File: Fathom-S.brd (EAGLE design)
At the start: 112.4 x 45.7 mm, 114 parts, among them IC1 LMH6643, IC2 LMH6643, IC3 ST490AB, IC4 ST490AB, IC5 FT230XS, Q1 BC817-40W, U1 MC7812, U2 MC7805, U4 INA139, U5 MC7805, X2 USBSMD

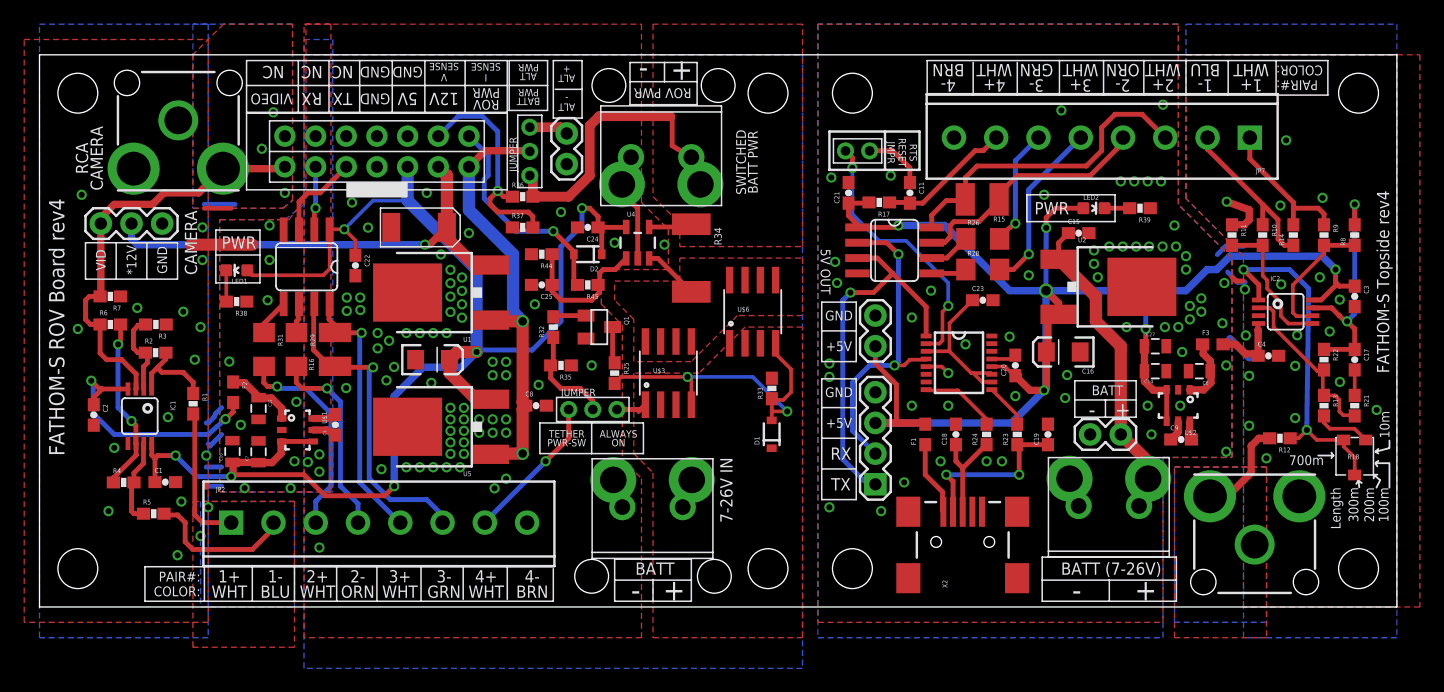
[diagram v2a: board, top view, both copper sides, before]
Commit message: Massive revision to simplify and make easier to use. Added DroneCode connectors, removed excessive stuff, and removed power switching.
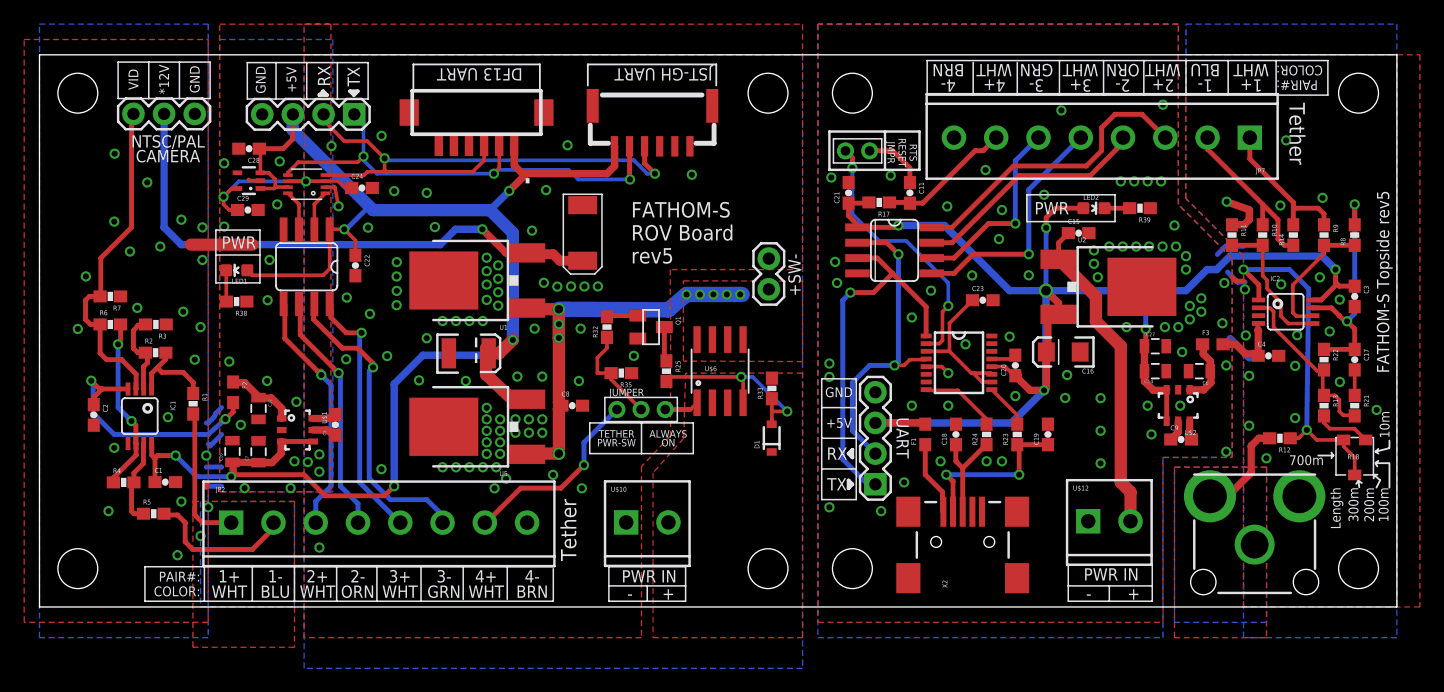
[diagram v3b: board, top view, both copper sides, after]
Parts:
- removed C25: 0.1uF, SparkFun-Passives:0603-CAP
- removed D2: Schottky, SparkFun-DiscreteSemi:SOD-323
- removed JP10, JP4, JP9: 0.1" HEADER, SparkFun-Connectors:1X02
- removed R15, R16: NP, resistor:R1210
- removed R26, R28, R29, R31: 0, SparkFun:1206
- removed R34: 0.001 1% 3W, SparkFun-Resistors:R2512
- removed R36: 18K 1%, SparkFun-Resistors:0603-RES
- removed R37: 2.2K 1%, SparkFun-Resistors:0603-RES
- removed R44: 68K 1%, SparkFun-Resistors:0603-RES
- removed R45: 1K, SparkFun-Resistors:0603-RES
- removed U$14: HEADER-33MM, BlueRobotics-Main:HEADER-2MM-3POS
- removed U4: INA139, SparkFun-AnalogIC:SOT23-5
- added C28, C29: 1uF, SparkFun-Passives:0603-CAP
- added JP5: M02PTH, SparkFun-Connectors:1X02
- added U$15: VREG-MIC5365, BlueRobotics-Main:SC70-5L
- C10: value 10uF 16V -> 47uF 10V; device SparkFun-Passives:EIA3216 -> SparkFun-Passives:EIA3528
- C24: device SparkFun-Passives:0603-CAP -> SparkFun:0603-CAP
- JP1: value PJRAN1X1U04X -> (none); device BlueRobotics-Main:RCA -> SparkFun-Connectors:1X04
- U$10, U$12: value HEADER-2 -> M023.5MM; device BR-Eagle-Library:TETHER-POWER-TERMINALS -> SparkFun-Connectors:SCREWTERMINAL-3.5MM-2
- U$11: value HEADER-2 -> JST-GH-6TOP-ENTRY; device BR-Eagle-Library:TETHER-POWER-TERMINALS -> BlueRobotics-JST-GH:JST-GH-TOP-6
- U$3: value Si4459ADY -> DF13-6P-1.25V; device SparkFun-DiscreteSemi:SO08 -> con-hirose-df13:DF13C-6P-1.25V
- U$6: value Si4459ADY -> AO4407A
- U$8: value TETHER-HEADERSERIAL -> TXS0102DCUR; device BR-Eagle-Library:TETHER-HEADER-2X7 -> BlueRobotics-Main:VSSOP-8
- moved U$4 47.9 mm to (35.1, -0.79), turned to 0 degrees
- moved U$9 25.9 mm to (5.73, 32.3)
- moved U$3 25.4 mm to (36.2, 39.1), turned to 180 degrees
- moved C24 19.0 mm to (26.7, 34.7), turned to 0 degrees
- moved JP1 14.6 mm to (26.1, 40.8), turned to 180 degrees
- moved C13 13.5 mm to (45.0, 31.0), turned to 90 degrees
- moved JP3 9.47 mm to (12.9, 40.8)
- moved U$6 5.61 mm to (56.4, 19.5)
- moved R35 5.04 mm to (48.2, 19.4)
- moved R32 4.45 mm to (47.0, 23.2)
- moved R25 4.29 mm to (51.9, 19.5)
- moved Q1 4.29 mm to (50.6, 23.2)
- moved U$8 4.00 mm to (23.7, 34.3), turned to 90 degrees
- moved U$13 4.00 mm to (47.8, 16.4)
- moved U1 3.16 mm to (35.1, 27.0)
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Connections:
- removed net I_SENSE: D2.A, R45.2, U$8.I_SENSE
- removed net N$23: IC3.5, R28.1
- removed net N$24: IC4.5, R31.1
- removed net N$25: IC4.6, R29.1
- removed net N$26: IC3.6, R26.1
- removed net N$33: C25.1, R44.1, R45.1, U4.1
- removed net ROV-ALT-VIN: JP10.1, U$14.P$3
- removed net ROV-VIN-PRESENSE: R34.2, U$3.5, U$3.6, U$3.7, U$3.8, U$6.5, U$6.6, U$6.7, U$6.8, U4.3
- removed net ROV-VIN-SWITCHED: R34.1, R36.2, U$11.1A, U$11.1B, U$14.P$1, U4.4
- removed net V_SENSE: R36.1, R37.2, U$8.V_SENSE
- new net 3.3V-ISO: C24.1, C29.1, U$15.5, U$8.3, U$8.6
- new net RX-3.3V: JP1.2, U$11.3, U$3.P$3, U$8.4
- new net TX-3.3V: JP1.1, U$11.2, U$3.P$2, U$8.5
- net 12V-ISO: no longer U$8.12V
- net CAMERA: no longer JP1.PIN, U$8.VIDEO
- net GND: now also U$12.1; no longer JP4.2, JP9.2, U$12.1A, U$12.1B
- net GND-ISO: now also C28.2, C29.2, JP1.4, JP5.1, U$10.1, U$11.6, U$15.2, U$3.P$6, U$8.2; no longer C25.2, JP1.SHELL, JP10.2, R37.1, R44.2, U$10.1A, U$10.1B, U$11.2A, U$11.2B, U$8.GND0, U$8.GND1, U$8.GND2, U4.2
- net N$28: no longer U$3.4
- net ROV-BATT: now also U$10.2; no longer U$10.2A, U$10.2B, U$3.1, U$3.2, U$3.3
- net ROV-RX: now also U$8.1; no longer U$8.RX
- net ROV-TP2+: now also IC4.5; no longer R31.2
- net ROV-TP2-: now also IC4.6; no longer R29.2
- net ROV-TP3+: no longer R16.2
- net ROV-TP3-: no longer R16.1
- net ROV-TX: now also U$8.8; no longer U$8.TX
- net ROV-VIN: now also JP5.2, U$6.5, U$6.6, U$6.7, U$6.8; no longer U$14.P$2, U$8.VBAT
- net TOP-TP2+: no longer R15.2
- net TOP-TP2-: no longer R15.1
- net TOP-TP3+: now also IC3.5; no longer R28.2
- net TOP-TP3-: now also IC3.6; no longer R26.2
- net TOP-VIN: now also U$12.2; no longer JP9.1, U$12.2A, U$12.2B
- net VCC: no longer JP4.1
- net VCC-ISO: now also C28.1, JP1.3, U$11.1, U$15.1, U$15.3, U$3.P$1, U$8.7; no longer C24.1, D2.C, U$8.5V, U4.5
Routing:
- net RX-3.3V: track 0.00 -> 48.5 mm, vias 0 -> 2
- net TX-3.3V: track 0.00 -> 39.5 mm, vias 0 -> 3
- net ROV-VIN-SWITCHED: track 26.4 -> 0.00 mm
- net VCC-ISO: track 121.3 -> 140.6 mm
- net V_SENSE: track 18.7 -> 0.00 mm, vias 1 -> 0
- net I_SENSE: track 18.2 -> 0.00 mm, vias 1 -> 0
- net 3.3V-ISO: track 0.00 -> 16.3 mm, vias 0 -> 2
- net N$33: track 12.0 -> 0.00 mm
- net N$28: track 27.7 -> 16.9 mm
- net CAMERA: track 35.3 -> 27.9 mm
- net 12V-ISO: track 39.0 -> 46.2 mm
- net VCC: track 125.1 -> 117.9 mm
- net TOP-TP3-: track 9.83 -> 16.0 mm
- net GND-ISO: track 20.6 -> 14.6 mm, vias 94 -> 109
- net TOP-TP3+: track 14.4 -> 20.1 mm
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- added copper zone on layer 1, net ROV-VIN
- removed copper zone on layer 1, net ROV-VIN-PRESENSE
- removed copper zone on layer 1, net ROV-VIN-SWITCHED
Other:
- board text added: "+SW-"
- board text added: "4/16"
- board text added: "DF13 UART"
- board text added: "DroneCode Mini Compatible"
- board text added: "FATHOM-S ROV Board rev5"
- board text added: "FATHOM-S Topside rev5"
- board text added: "JST-GH UART"
- board text added: "NTSC/PAL CAMERA"
- board text added: "PWR IN"
- board text added: "Tether"
- board text added: "UART"
- board text removed: "12/15"
- board text removed: "12V"
- board text removed: "5V"
- board text removed: "5V OUT"
- board text removed: "7-26V IN"
- board text removed: "ALT +"
- board text removed: "ALT -"
- board text removed: "ALT PWR"
- board text removed: "BATT"
- board text removed: "BATT (7-26V)"
- board text removed: "BATT PWR"
- board text removed: "CAMERA"
- board text removed: "FATHOM-S ROV Board rev4"
- board text removed: "FATHOM-S Topside rev4"
- board text removed: "I SENSE"
- board text removed: "NC"
- board text removed: "RCA CAMERA"
- board text removed: "ROV PWR"
- board text removed: "SWITCHED BATT PWR"
- board text removed: "V SENSE"
- board text removed: "VIDEO"

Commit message: Change 12V output capacitor size.
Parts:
- C13: value 10uF 25V -> 33uF 20V
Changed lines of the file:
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@@
 <attribute name="VALUE" value="3.3V" x="60.6275" y="13.985" size="1.778" layer="27" rot="R90" display="off"/>
 </element>
-<element name="C13" library="SparkFun-Passives" package="EIA6032" value="10uF 25V" x="44.97375" y="30.9725" rot="R90"/>
+<element name="C13" library="SparkFun-Passives" package="EIA6032" value="33uF 20V" x="44.97375" y="30.9725" rot="R90"/>
 <element name="JP3" library="SparkFun-Connectors" package="1X03" value="0.1&quot; HEADER" x="12.85875" y="40.83" smashed="yes" rot="R180"/>
 <element name="U$6" library="SparkFun-DiscreteSemi" package="SO08" value=" AO4407A " x="56.35625" y="19.52625"/>

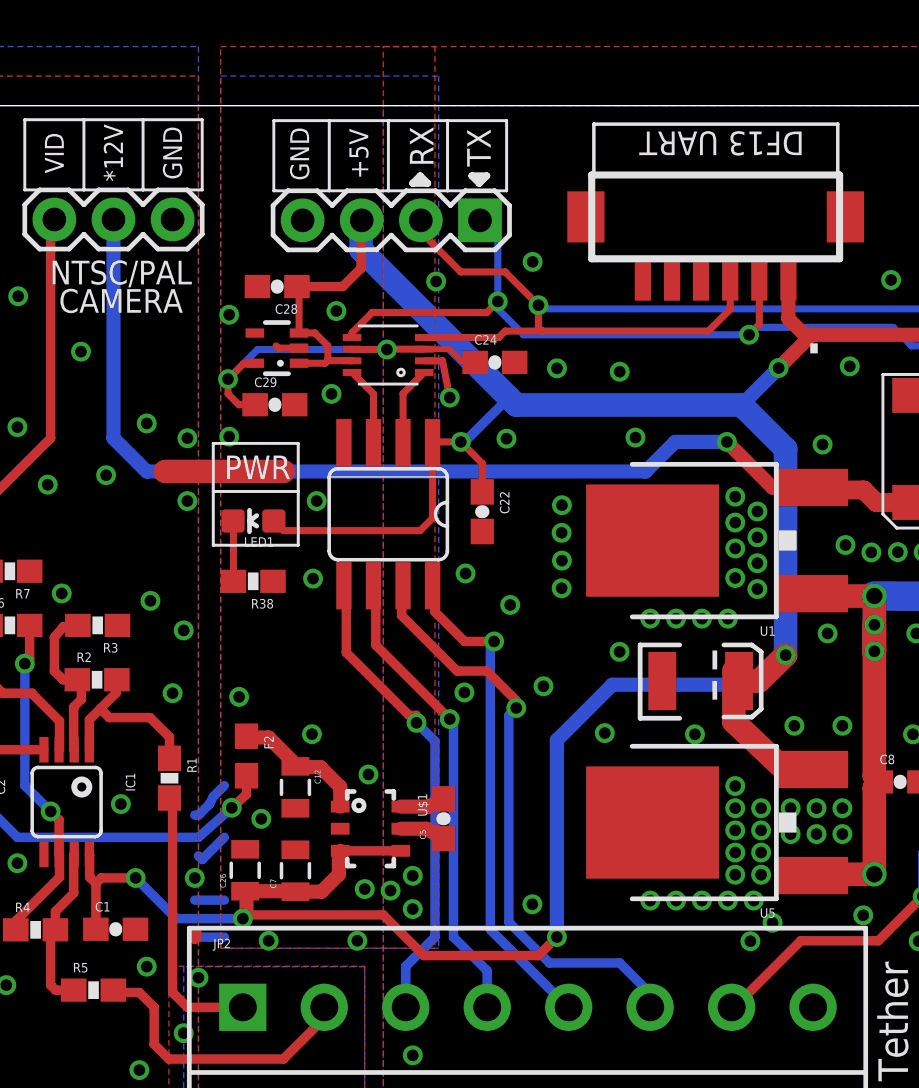
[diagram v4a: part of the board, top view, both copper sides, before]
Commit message: Switch to FET based level shifting for 5V tolerance.
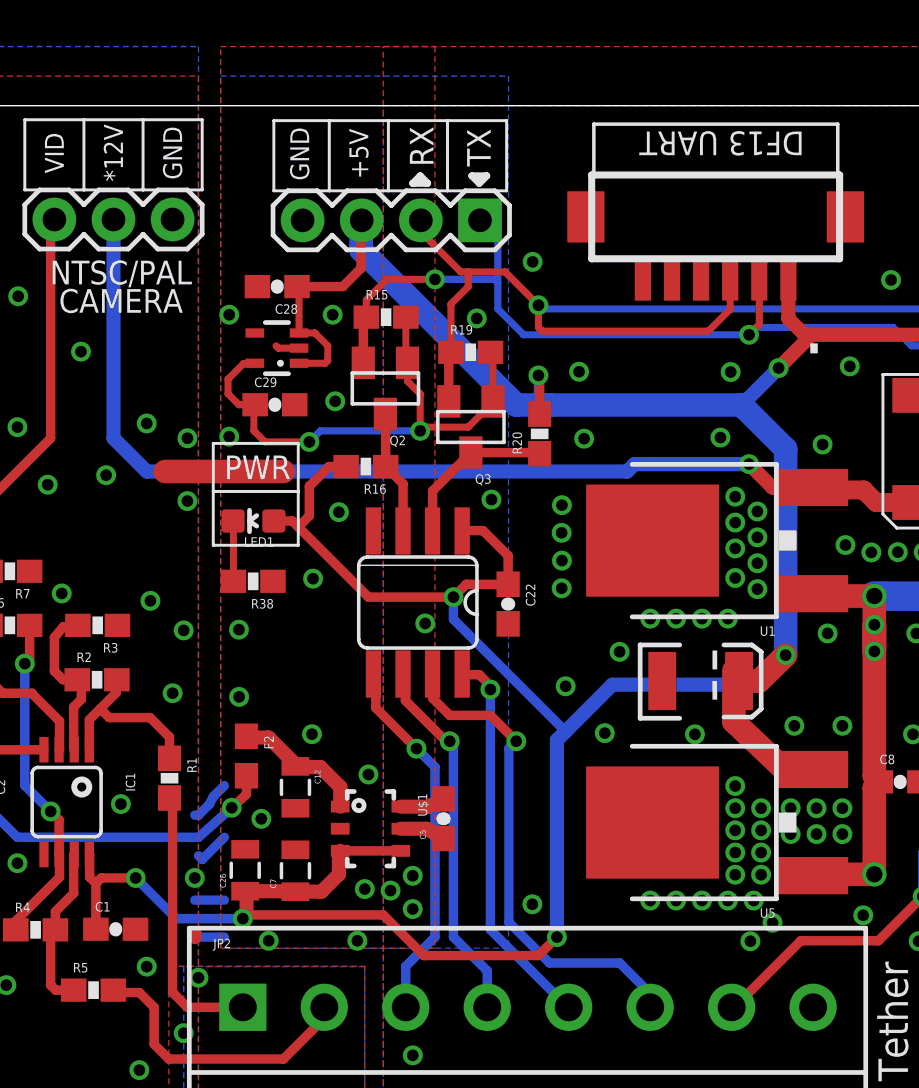
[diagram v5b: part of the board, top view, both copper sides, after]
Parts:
- removed C24: 0.1uF, SparkFun:0603-CAP
- removed U$8: TXS0102DCUR, BlueRobotics-Main:VSSOP-8
- added Q2, Q3: BSS138, SparkFun-DiscreteSemi:SOT23
- added R15, R16, R19, R20: 10K, SparkFun:0603-RES
- moved C22 4.12 mm to (27.3, 24.3)
- moved IC4 4.00 mm to (23.4, 24.4)
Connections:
- net 3.3V-ISO: now also Q2.1, Q3.1, R15.2, R19.2; no longer C24.1, U$8.3, U$8.6
- net GND-ISO: no longer C24.2, U$8.2
- net ROV-RX: now also Q3.3, R20.1; no longer U$8.1
- net ROV-TX: now also Q2.3, R16.1; no longer U$8.8
- net RX-3.3V: now also Q3.2, R19.1; no longer U$8.4
- net TX-3.3V: now also Q2.2, R15.1; no longer U$8.5
- net VCC-ISO: now also R16.2, R20.2; no longer U$8.7
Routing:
- net VCC-ISO: track 140.6 -> 152.6 mm, vias 6 -> 7
- net 3.3V-ISO: track 16.3 -> 23.1 mm
- net ROV-TP3+: track 21.5 -> 16.6 mm
- net ROV-TP2+: track 20.5 -> 15.9 mm
- net ROV-TP2-: track 20.2 -> 15.9 mm
- net ROV-TP3-: track 25.3 -> 21.2 mm
- net ROV-RX: track 3.39 -> 7.02 mm
- net GND-ISO: track 14.6 -> 12.2 mm, vias 109 -> 108
- net ROV-TX: track 3.40 -> 5.34 mm
- net TX-3.3V: track 39.5 -> 41.3 mm
- net 12V-ISO: track 46.2 -> 45.5 mm
- net RX-3.3V: track 48.5 -> 49.2 mm

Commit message: Further updates to Rev5. First production run.
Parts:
- added TP1, TP6: -5V, BlueRobotics-Main:B1,27
- added TP2: 12V, BlueRobotics-Main:B1,27
- added TP3, TP5: 5V, BlueRobotics-Main:B1,27
- added TP4: VIN, BlueRobotics-Main:B1,27
- moved U$9 45.4 mm to (51.1, 33.6), turned to 270 degrees
- moved U$12 0.16 mm to (86.8, 6.94)
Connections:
- net -VCC: now also TP6.TP
- net -VCC-ISO: now also TP1.TP
- net 12V-ISO: now also TP2.TP
- net ROV-VIN: now also TP4.TP
- net VCC: now also TP5.TP
- net VCC-ISO: now also TP3.TP
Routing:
- net 12V-ISO: track 45.5 -> 49.0 mm, vias 1 -> 2
- net -VCC: track 6.08 -> 9.17 mm
- net -VCC-ISO: track 21.6 -> 24.1 mm
- net VCC: track 117.9 -> 120.2 mm
- net VCC-ISO: track 152.6 -> 154.3 mm
- net GND: vias 83 -> 84

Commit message: Updated files before release.
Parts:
- C13: device SparkFun-Passives:EIA6032 -> BlueRobotics-Main:C2413
- moved C13 3.24 mm to (45.6, 27.8)
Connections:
- net 12V-ISO: now also C13.+; no longer C13.P$1
- net GND-ISO: now also C13.-; no longer C13.P$2
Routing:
- net 12V-ISO: track 49.0 -> 50.0 mm
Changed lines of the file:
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@@
 <attribute name="VALUE" value="3.3V" x="60.6275" y="13.985" size="1.778" layer="27" rot="R90" display="off"/>
 </element>
-<element name="C13" library="SparkFun-Passives" package="EIA6032" value="33uF 20V" x="44.97375" y="30.9725" rot="R90"/>
+<element name="C13" library="BlueRobotics-Main" package="C2413" value="33uF 20V" x="45.60875" y="27.7975" rot="R90"/>
 <element name="JP3" library="SparkFun-Connectors" package="1X03" value="0.1&quot; HEADER" x="12.85875" y="40.83" smashed="yes" rot="R180"/>
 <element name="U$6" library="SparkFun-DiscreteSemi" package="SO08" value=" AO4407A " x="56.35625" y="19.52625"/>
@@
 <contactref element="JP2" pad="8"/>
 <contactref element="Q1" pad="2"/>
-<contactref element="C13" pad="P$2"/>
+<contactref element="C13" pad="-"/>
 <contactref element="JP3" pad="1"/>
 <contactref element="R38" pad="1"/>
@@
 <vertex x="21.11375" y="-3.33375"/>
 </polygon>
-<polygon width="0.4064" layer="16" isolate="0.254">
+<polygon width="0.4064" layer="16" isolate="0.254" thermals="no">
 <vertex x="21.9075" y="45.72"/>
 <vertex x="63.1825" y="45.72"/>
@@
 <via x="40.7825" y="31.1625" extent="1-16" drill="0.5"/>
 <contactref element="U$10" pad="1"/>
-<polygon width="0.4064" layer="1" isolate="0.254">
+<polygon width="0.4064" layer="1" isolate="0.254" thermals="no">
 <vertex x="21.9075" y="48.26"/>
 <vertex x="63.1825" y="48.26"/>
@@
 <via x="34.48965" y="11.5697" extent="1-16" drill="0.5"/>
 <via x="44.6659" y="18.71345" extent="1-16" drill="0.5"/>
-<via x="44.01465" y="26.5397" extent="1-16" drill="0.5"/>
+<via x="49.09465" y="26.5397" extent="1-16" drill="0.5"/>
 <via x="37.98215" y="27.1747" extent="1-16" drill="0.5"/>
 <via x="23.1775" y="4.92125" extent="1-16" drill="0.5"/>
@@
 <via x="42.87715" y="26.5272" extent="1-16" drill="0.5"/>
 <via x="41.7659" y="26.8447" extent="1-16" drill="0.5"/>
-<via x="45.1259" y="26.5397" extent="1-16" drill="0.5"/>
-<via x="46.23715" y="26.5397" extent="1-16" drill="0.5"/>
+<via x="50.2059" y="26.5397" extent="1-16" drill="0.5"/>
+<via x="51.31715" y="26.5397" extent="1-16" drill="0.5"/>
 </signal>
 <signal name="VCC-ISO">
@@
 <contactref element="U$6" pad="6"/>
 <contactref element="U$6" pad="7"/>
-<polygon width="0.4064" layer="1" isolate="0.254">
+<polygon width="0.4064" layer="1" isolate="0.254" thermals="no">
 <vertex x="53.3175" y="20.365"/>
 <vertex x="53.3175" y="27"/>
@@
 </signal>
 <signal name="12V-ISO">
-<contactref element="C13" pad="P$1"/>
+<contactref element="C13" pad="+"/>
 <contactref element="JP3" pad="2"/>
 <contactref element="U1" pad="3"/>
@@
 <wire x1="10.31875" y1="31.4325" x2="10.31875" y2="33.655" width="0.6096" layer="16"/>
 <wire x1="10.31875" y1="33.655" x2="10.31875" y2="40.83" width="0.6096" layer="16"/>
-<wire x1="44.97375" y1="28.6725" x2="43.0825" y2="28.6725" width="0.8128" layer="1"/>
-<wire x1="43.0825" y1="28.6725" x2="42.545" y2="29.21" width="0.8128" layer="1"/>
+<wire x1="45.60875" y1="27.7975" x2="43.87625" y2="27.87875" width="0.8128" layer="1"/>
+<wire x1="43.87625" y1="27.87875" x2="42.545" y2="29.21" width="0.8128" layer="1"/>
 <wire x1="42.545" y1="29.21" x2="40.4825" y2="29.21" width="0.8128" layer="1"/>
 <wire x1="40.4825" y1="29.21" x2="40.3775" y2="29.315" width="0.8128" layer="1"/>
@@
 <contactref element="U$6" pad="2"/>
 <contactref element="U$6" pad="1"/>
-<polygon width="0.4064" layer="1" isolate="0.254">
+<polygon width="0.4064" layer="1" isolate="0.254" thermals="no">
 <vertex x="50.8" y="-2.54"/>
 <vertex x="63.1825" y="-2.54"/>
